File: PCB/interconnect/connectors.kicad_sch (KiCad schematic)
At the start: 15 parts, among them J201 XT60-M, J202 5.08mm Screw Terminal, J203 Conn_01x03, J204 Conn_01x03, J205 Conn_01x03, J206 Conn_01x04, Q201 AO3400A

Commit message: PCB Rev 1
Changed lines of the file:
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@@
+	(wire
+		(pts
+			(xy 153.67 91.44) (xy 153.67 92.71)
+		)
+		(stroke
+			(width 0)
+			(type default)
+		)
+	)
 	(wire
 		(pts
@@
 	(wire
 		(pts
+			(xy 55.88 173.99) (xy 73.66 173.99)
+		)
+		(stroke
+			(width 0)
+			(type default)
+		)
+	)
+	(wire
+		(pts
 			(xy 93.98 57.15) (xy 50.8 57.15)
 		)
@@
 		)
 	)
+	(wire
+		(pts
+			(xy 55.88 168.91) (xy 73.66 168.91)
+		)
+		(stroke
+			(width 0)
+			(type default)
+		)
+	)
 	(bus
 		(pts
@@
 	(wire
 		(pts
+			(xy 153.67 91.44) (xy 154.94 91.44)
+		)
+		(stroke
+			(width 0)
+			(type default)
+		)
+	)
+	(wire
+		(pts
 			(xy 147.32 57.15) (xy 170.18 57.15)
 		)
@@
 		(pts
 			(xy 66.04 152.4) (xy 64.77 152.4)
+		)
+		(stroke
+			(width 0)
+			(type default)
+		)
+	)
+	(wire
+		(pts
+			(xy 55.88 171.45) (xy 73.66 171.45)
 		)
 		(stroke
@@
 	)
 	(label "MOTORS.Magnet"
-		(at 55.88 173.99 0)
-		(effects
-			(font
-				(size 1.27 1.27)
-			)
-			(justify left bottom)
+		(at 73.66 173.99 180)
+		(effects
+			(font
+				(size 1.27 1.27)
+			)
+			(justify right bottom)
 		)
 	)
@@
 	)
 	(label "MOTORS.Steering"
-		(at 55.88 171.45 0)
-		(effects
-			(font
-				(size 1.27 1.27)
-			)
-			(justify left bottom)
+		(at 73.66 171.45 180)
+		(effects
+			(font
+				(size 1.27 1.27)
+			)
+			(justify right bottom)
 		)
 	)
@@
 	)
 	(label "MOTORS.ESC"
-		(at 55.88 168.91 0)
-		(effects
-			(font
-				(size 1.27 1.27)
-			)
-			(justify left bottom)
+		(at 73.66 168.91 180)
+		(effects
+			(font
+				(size 1.27 1.27)
+			)
+			(justify right bottom)
 		)
 	)
@@
 	(symbol
 		(lib_id "power:GND")
-		(at 154.94 91.44 0)
+		(at 153.67 92.71 0)
 		(unit 1)
 		(exclude_from_sim no)
@@
 		(fields_autoplaced yes)
 		(property "Reference" "#PWR0201"
-			(at 154.94 97.79 0)
+			(at 153.67 99.06 0)
 			(effects
 				(font
@@
 		)
 		(property "Value" "GND"
-			(at 154.94 96.52 0)
+			(at 153.67 97.79 0)
 			(effects
 				(font
@@
 		)
 		(property "Footprint" ""
-			(at 154.94 91.44 0)
+			(at 153.67 92.71 0)
 			(effects
 				(font
@@
 		)
 		(property "Datasheet" ""
-			(at 154.94 91.44 0)
+			(at 153.67 92.71 0)
 			(effects
 				(font
@@
 		)
 		(property "Description" "Power symbol creates a global label with name \"GND\" , ground"
-			(at 154.94 91.44 0)
-			(effects
-				(font
+			(at 153.67 92.71 0)
+			(effects
+				(font

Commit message: Order
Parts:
- J201, J202, J203, J204, J205, J206: now not fitted
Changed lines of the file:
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@@
 		(in_bom yes)
 		(on_board yes)
-		(dnp no)
+		(dnp yes)
 		(fields_autoplaced yes)
 		(property "Reference" "J201"
@@
 		(in_bom yes)
 		(on_board yes)
-		(dnp no)
+		(dnp yes)
 		(property "Reference" "J202"
 			(at 179.324 139.192 0)
@@
 		(in_bom yes)
 		(on_board yes)
-		(dnp no)
+		(dnp yes)
 		(property "Reference" "J203"
 			(at 73.66 148.5899 0)
@@
 		(in_bom yes)
 		(on_board yes)
-		(dnp no)
+		(dnp yes)
 		(property "Reference" "J205"
 			(at 113.03 158.496 0)
@@
 		(in_bom yes)
 		(on_board yes)
-		(dnp no)
+		(dnp yes)
 		(fields_autoplaced yes)
 		(property "Reference" "J206"
@@
 		(in_bom yes)
 		(on_board yes)
-		(dnp no)
+		(dnp yes)
 		(property "Reference" "J204"
 			(at 113.03 134.366 0)

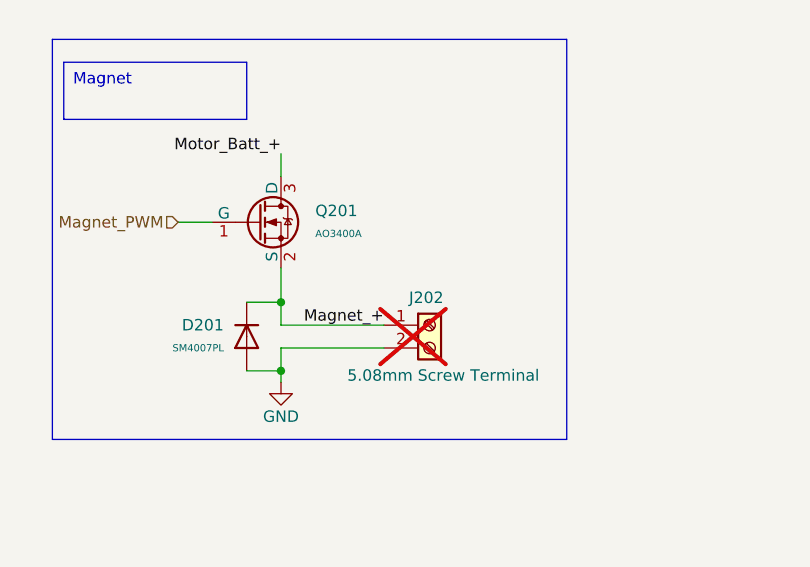
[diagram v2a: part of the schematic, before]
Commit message: Updated PCB, working inference
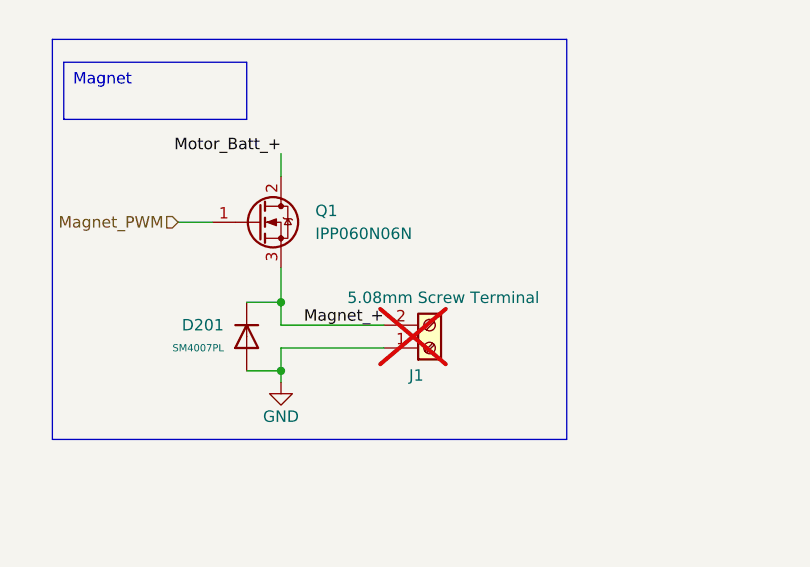
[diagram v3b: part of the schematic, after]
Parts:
- removed J202: 5.08mm Screw Terminal, TerminalBlock_Phoenix:TerminalBlock_Phoenix_MKDS-1,5-2-5.08_1x02_P5.08mm_Horizontal, symbol Connector:Screw_Terminal_01x02
- removed Q201: AO3400A, PCM_JLCPCB:Q_SOT-23, symbol PCM_JLCPCB-Transistors:NMOS,AO3400A
- added J1: 5.08mm Screw Terminal, TerminalBlock_Phoenix:TerminalBlock_Phoenix_MKDS-1,5-2-5.08_1x02_P5.08mm_Horizontal, symbol Connector:Screw_Terminal_01x02
- added Q1: IPP060N06N, Package_TO_SOT_THT:TO-220-3_Vertical, symbol Transistor_FET:IPP060N06N
- C201, C202, C203: footprint PCM_JLCPCB:C_0805 -> Capacitor_THT:C_Disc_D5.0mm_W2.5mm_P2.50mm
- D201: footprint PCM_JLCPCB:D_SOD-123FL -> Diode_THT:D_5W_P10.16mm_Horizontal
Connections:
- net GND: now also J1.1 (Pin_1)
- net Magnet_+: now also J1.2 (Pin_2), Q1.3 (S)
- net Magnet_PWM: now also Q1.1 (G)
- net Motor_Batt_+: now also Q1.2 (D)
